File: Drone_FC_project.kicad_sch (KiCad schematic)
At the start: 1 part, among them U2 STM32F103C8Tx

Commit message: IMU
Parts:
- removed U2: STM32F103C8Tx, Package_QFP:LQFP-48_7x7mm_P0.5mm, symbol MCU_ST_STM32F1:STM32F103C8Tx
- added U2: STM32F411CCUx, Package_DFN_QFN:QFN-48-1EP_7x7mm_P0.5mm_EP5.6x5.6mm, symbol MCU_ST_STM32F4:STM32F411CCUx
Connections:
- new net: U2.23 (VSS), U2.35 (VSS), U2.47 (VSS), U2.49 (VSS)
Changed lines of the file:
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@@
 	(paper "A4")
 	(symbol
-		(lib_id "MCU_ST_STM32F1:STM32F103C8Tx")
-		(at 106.68 81.28 0)
+		(lib_id "MCU_ST_STM32F4:STM32F411CCUx")
+		(at 99.06 80.01 0)
 		(unit 1)
 		(body_style 1)
@@
 		(fields_autoplaced yes)
 		(property "Reference" "U2"
-			(at 111.3633 121.92 0)
-			(show_name no)
-			(do_not_autoplace no)
-			(effects
-				(font
-					(size 1.27 1.27)
-				)
-				(justify left)
-			)
-		)
-		(property "Value" "STM32F103C8Tx"
-			(at 111.3633 124.46 0)
-			(show_name no)
-			(do_not_autoplace no)
-			(effects
-				(font
-					(size 1.27 1.27)
-				)
-				(justify left)
-			)
-		)
-		(property "Footprint" "Package_QFP:LQFP-48_7x7mm_P0.5mm"
-			(at 91.44 119.38 0)
+			(at 103.7433 120.65 0)
+			(show_name no)
+			(do_not_autoplace no)
+			(effects
+				(font
+					(size 1.27 1.27)
+				)
+				(justify left)
+			)
+		)
+		(property "Value" "STM32F411CCUx"
+			(at 103.7433 123.19 0)
+			(show_name no)
+			(do_not_autoplace no)
+			(effects
+				(font
+					(size 1.27 1.27)
+				)
+				(justify left)
+			)
+		)
+		(property "Footprint" "Package_DFN_QFN:QFN-48-1EP_7x7mm_P0.5mm_EP5.6x5.6mm"
+			(at 83.82 118.11 0)
 			(hide yes)
 			(show_name no)
@@
 			)
 		)
-		(property "Datasheet" "https://www.st.com/resource/en/datasheet/stm32f103c8.pdf"
-			(at 106.68 81.28 0)
+		(property "Datasheet" "https://www.st.com/resource/en/datasheet/stm32f411cc.pdf"
+			(at 99.06 80.01 0)
 			(hide yes)
 			(show_name no)
@@
 			)
 		)
-		(property "Description" "STMicroelectronics Arm Cortex-M3 MCU, 64KB flash, 20KB RAM, 72 MHz, 2.0-3.6V, 37 GPIO, LQFP48"
-			(at 106.68 81.28 0)
+		(property "Description" "STMicroelectronics Arm Cortex-M4 MCU, 256KB flash, 128KB RAM, 100 MHz, 1.7-3.6V, 36 GPIO, UFQFPN48"
+			(at 99.06 80.01 0)
 			(hide yes)
 			(show_name no)
@@
 			)
 		)
+		(pin "21"
+		)
+		(pin "10"
+		)
+		(pin "22"
+		)
+		(pin "2"
+		)
+		(pin "11"
+		)
+		(pin "18"
+		)
+		(pin "27"
+		)
+		(pin "17"
+		)
+		(pin "8"
+		)
+		(pin "32"
+		)
+		(pin "30"
+		)
+		(pin "14"
+		)
+		(pin "1"
+		)
+		(pin "5"
+		)
+		(pin "7"
+		)
+		(pin "23"
+		)
+		(pin "24"
+		)
+		(pin "12"
+		)
+		(pin "9"
+		)
+		(pin "29"
+		)
+		(pin "20"
+		)
+		(pin "28"
+		)
+		(pin "16"
+		)
+		(pin "15"
+		)
+		(pin "19"
+		)
+		(pin "13"
+		)
+		(pin "26"
+		)
+		(pin "25"
+		)
+		(pin "6"
+		)
 		(pin "3"
 		)
-		(pin "8"
-		)
-		(pin "6"
-		)
-		(pin "5"
-		)
-		(pin "10"
-		)
 		(pin "4"
 		)
-		(pin "2"
-		)
-		(pin "12"
-		)
-		(pin "7"
-		)
-		(pin "11"
-		)
-		(pin "9"
-		)
-		(pin "1"
-		)
-		(pin "13"
-		)
-		(pin "15"
-		)
 		(pin "31"
 		)
-		(pin "23"
-		)
-		(pin "29"
-		)
-		(pin "16"
+		(pin "38"
+		)
+		(pin "46"
+		)
+		(pin "41"
+		)
+		(pin "47"
+		)
+		(pin "36"
+		)
+		(pin "34"
+		)
+		(pin "39"
+		)
+		(pin "42"
 		)
 		(pin "35"
 		)
+		(pin "48"
+		)
+		(pin "40"
+		)
+		(pin "49"
+		)
+		(pin "45"
+		)
+		(pin "43"
+		)
+		(pin "44"
+		)
+		(pin "33"
+		)
 		(pin "37"
-		)
-		(pin "18"
-		)
-		(pin "27"
-		)
-		(pin "32"
-		)
-		(pin "19"
-		)
-		(pin "38"
-		)
-		(pin "28"
-		)
-		(pin "43"
-		)
-		(pin "36"
-		)
-		(pin "39"
-		)
-		(pin "42"
-		)
-		(pin "20"
-		)
-		(pin "21"
-		)
-		(pin "41"
-		)
-		(pin "24"
-		)
-		(pin "40"
-		)
-		(pin "33"
-		)
-		(pin "45"
-		)
-		(pin "14"
-		)
-		(pin "44"
-		)
-		(pin "30"
-		)
-		(pin "25"
-		)
-		(pin "22"
-		)
-		(pin "17"
-		)
-		(pin "26"
-		)
-		(pin "34"
-		)
-		(pin "47"
-		)
-		(pin "48"
-		)
-		(pin "46"
 		)
 		(instances
@@
 	)
 	(sheet
-		(at 39.37 74.93)
+		(at 24.13 130.81)
 		(size 12.7 5.08)
 		(exclude_from_sim no)
@@
 		)
 		(property "Sheetname" "Battery and regulator"
-			(at 39.37 74.2184 0)
+			(at 24.13 130.0984 0)
 			(show_name no)
 			(do_not_autoplace no)
@@
 		)
 		(property "Sheetfile" "Battery_and_regulator.kicad_sch"
-			(at 39.37 80.5946 0)
-			(show_name no)
-			(do_not_autoplace no)
+			(at 24.13 136.4746 0)
+			(show_name no)
+			(do_not_autoplace no)

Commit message: Updated stm32
Updated stm32 and usb-c
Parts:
- removed U2: STM32F411CCUx, Package_DFN_QFN:QFN-48-1EP_7x7mm_P0.5mm_EP5.6x5.6mm, symbol MCU_ST_STM32F4:STM32F411CCUx
- added C1, C11, C2, C3, C4: 100n, Capacitor_SMD:C_0603_1608Metric, symbol Device:C
- added C10, C9: 1u, Package_TO_SOT_SMD:SOT-23-5, symbol Device:C
- added C12, C13: 10p, Capacitor_SMD:C_0603_1608Metric, symbol Device:C
- added C5: 1u, Package_SO:SOIC-8_3.9x4.9mm_P1.27mm, symbol Device:C
- added C6: 4.7u, Package_SO:SOIC-8_3.9x4.9mm_P1.27mm, symbol Device:C
- added C7: 100n, Package_SO:SOIC-8_3.9x4.9mm_P1.27mm, symbol Device:C
- added D5, D6: LED, symbol Device:LED
- added J5: Conn_01x04_Pin, Package_DIP:DIP-6_W7.62mm, symbol Connector:Conn_01x04_Pin
- added J6: USB_C_Receptacle, symbol Connector:USB_C_Receptacle_USB2.0_16P
- added R10, R9: 1k, symbol Device:R
- added R11, R12: 5k1, symbol Device:R
- added R13: 10k, Package_TO_SOT_SMD:SOT-23, symbol Device:R
- added SW2: SW_Push, Button_Switch_THT:SW_NKK_GW12LJP, symbol Switch:SW_Push
- added TP1, TP2: TestPoint, RF_Module:Atmel_ATSAMR21G18-MR210UA_NoRFPads, symbol Connector:TestPoint
- added U3: AP2112K-3.3TRG1, Package_TO_SOT_SMD:SOT-23-5, symbol Regulator_Linear:AP2112K-3.3
- added U4: STM32F411CEU6, Package_DFN_QFN:QFN-48-1EP_7x7mm_P0.5mm_EP5.6x5.6mm, symbol MCU_ST_STM32F4:STM32F411CEUx
- added Y1: 8MHz, symbol Device:Crystal_GND24
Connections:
- new net: D5.1 (K), R9.1
- new net: J6.B5 (CC2), R12.1
- new net: J6.A4 (VBUS), J6.A9 (VBUS), J6.B4 (VBUS), J6.B9 (VBUS)
- new net: J6.A5 (CC1), R11.1
- new net: J6.A6 (D+), J6.B6 (D+), U4.33 (PA12)
- new net: J6.A7 (D-), J6.B7 (D-), U4.32 (PA11)
- new net: D6.1 (K), R10.1
- new net: U4.23 (VSS), U4.35 (VSS), U4.47 (VSS), U4.49 (VSS)
- new net: TP1.1, U4.34 (PA13)
- new net: TP2.1, U4.37 (PA14)
- new net: C12.1, U4.5 (PH0), Y1.1
- new net: C13.1, U4.6 (PH1), Y1.3
- new net +3.3V: C1.1, C10.1, C2.1, C3.1, C4.1, C5.1, C6.1, C7.1, D5.2 (A), SW2.1, U3.5 (VOUT), U4.1 (VBAT), U4.24 (VDD), U4.36 (VDD), U4.48 (VDD), U4.9 (VDDA)
- new net +5V: D6.2 (A)
- new net +BATT: C9.1, J5.1 (Pin_1), J5.2 (Pin_2), U3.1 (VIN), U3.3 (EN)
- new net BOOT0: R13.1, SW2.2, U4.44 (BOOT0)
- new net GND: C1.2, C10.2, C11.2, C12.2, C13.2, C2.2, C3.2, C4.2, C5.2, C6.2, C7.2, C9.2, J5.3 (Pin_3), J5.4 (Pin_4), J6.A1 (GND), J6.A12 (GND), J6.B1 (GND), J6.B12 (GND), J6.SH (SHIELD), R10.2, R11.2, R12.2, R13.2, R9.2, U3.2 (GND), Y1.2 (G), Y1.4 (G)
- new net NRST: C11.1, U4.7 (NRST)
- no-connect marks 0 -> 3
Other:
- note added: "RED LEDs To inidicate 3.3V/5V is running"
- note added: "The pins that attach to the battery"
- note added: "Tie EN to HIGH"

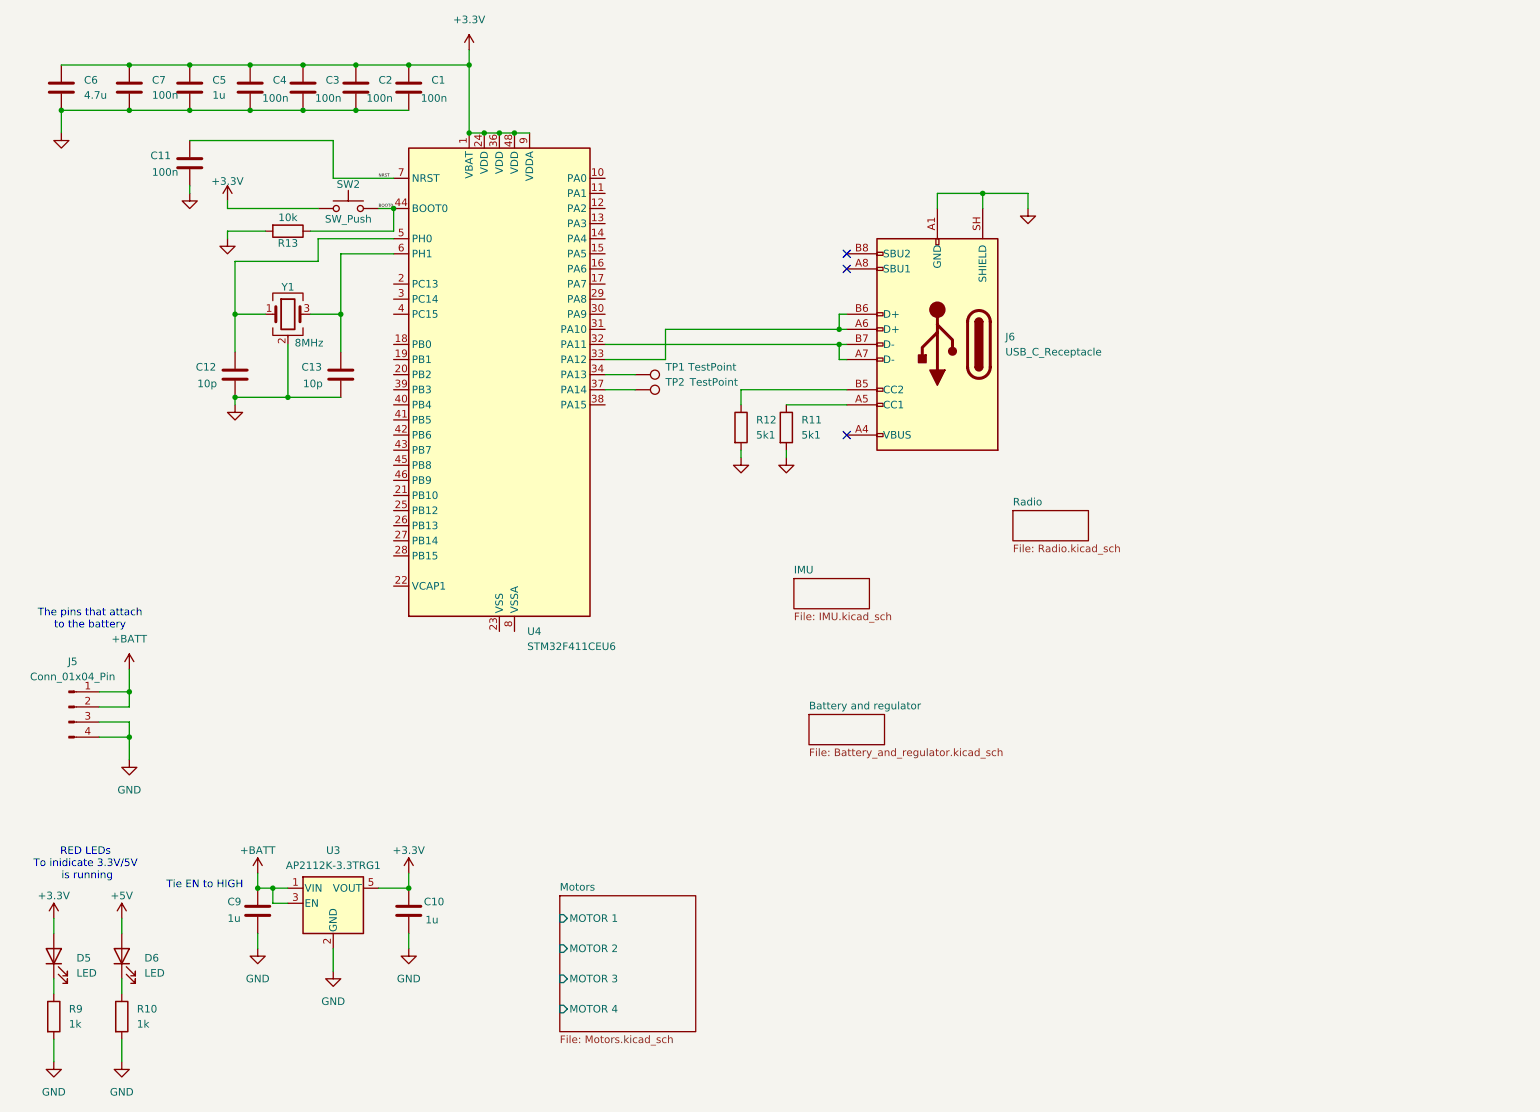
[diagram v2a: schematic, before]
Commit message: IMU, VBAT_Sense,
Fixed some decoupling issues, made the IMU into SPI mode. Wired all to stm32. Few updates on the appearances as well to make it look more organized.
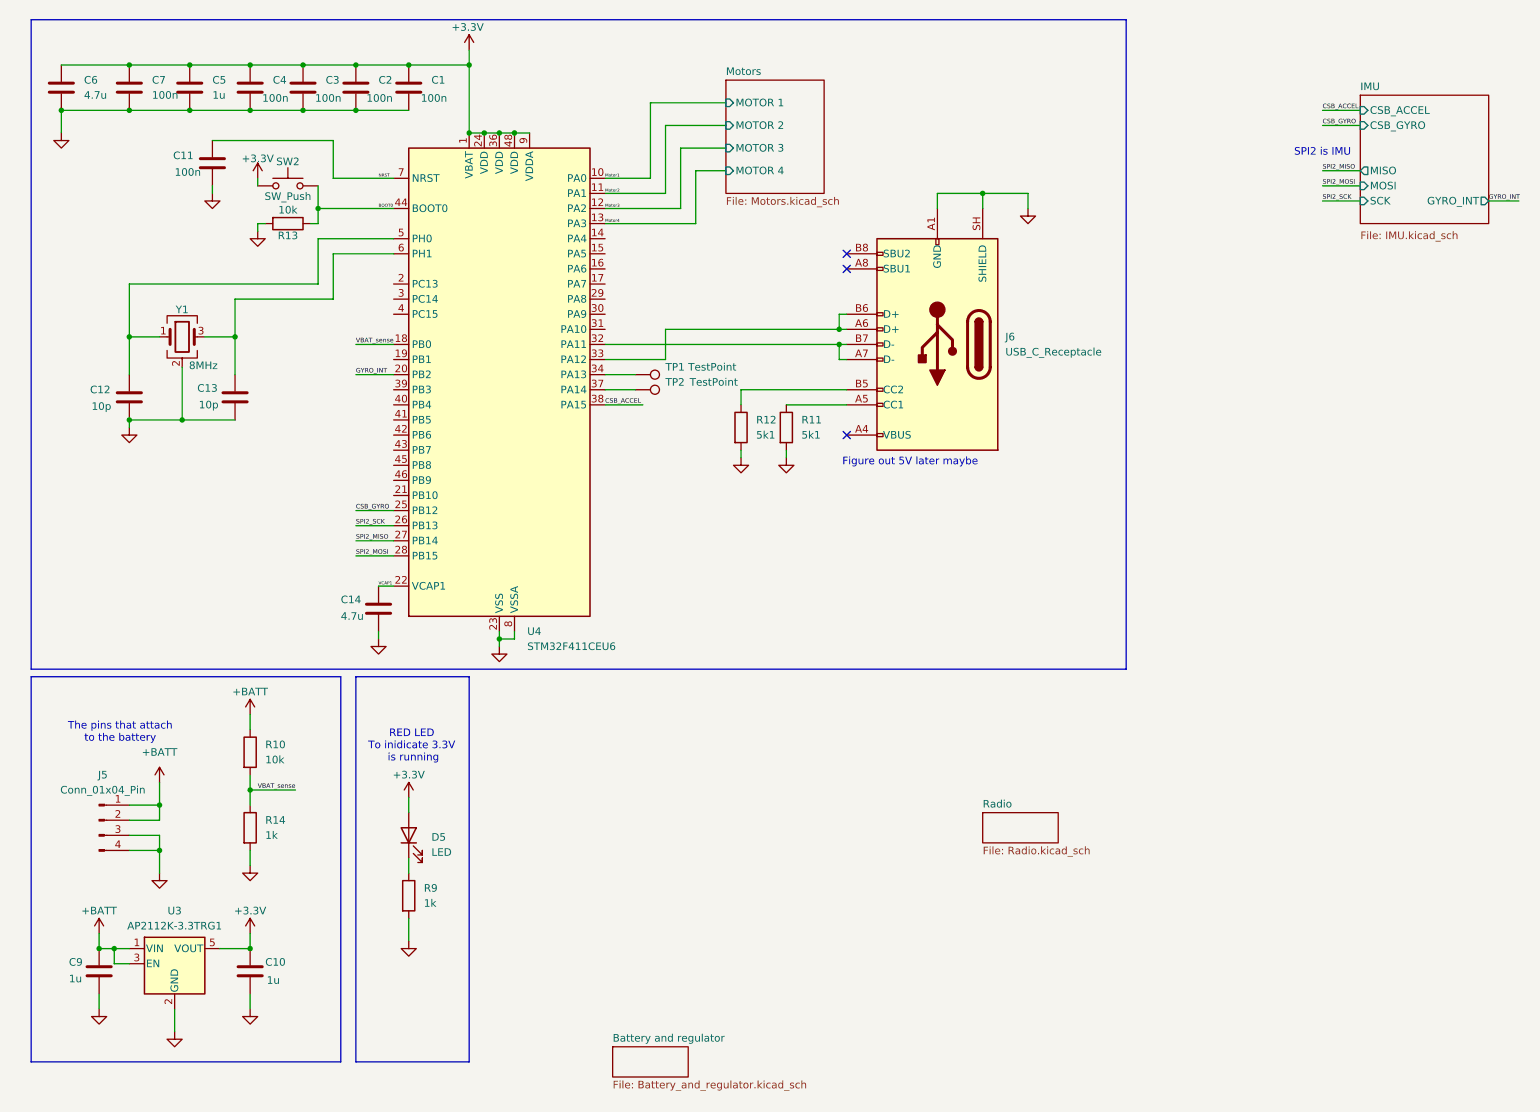
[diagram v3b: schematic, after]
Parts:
- removed D6: LED, symbol Device:LED
- added C14: 4.7u, Package_SO:SOIC-8_3.9x4.9mm_P1.27mm, symbol Device:C
- added R14: 1k, symbol Device:R
- R10: value 1k -> 10k
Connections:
- net +BATT: now also R10.1
- net GND: now also U4.23 (VSS), U4.35 (VSS), U4.47 (VSS), U4.49 (VSS), U4.8 (VSSA), C14.2, R14.2; no longer R10.2
- net Motor1: now reaches U4.10 (PA0)
- net Motor2: now reaches U4.11 (PA1)
- net Motor3: now reaches U4.12 (PA2)
- net Motor4: now reaches U4.13 (PA3)
- net VBAT_sense: now reaches U4.18 (PB0)
- net VBAT_sense: now also R10.2, R14.1
- net GYRO_INT: now reaches U4.20 (PB2)
- net VCAP1: now reaches U4.22 (VCAP1)
- net VCAP1: now also C14.1
- net CSB_GYRO: now reaches U4.25 (PB12)
- net SPI2_SCK: now reaches U4.26 (PB13)
- net SPI2_MISO: now reaches U4.27 (PB14)
- net SPI2_MOSI: now reaches U4.28 (PB15)
- net CSB_ACCEL: now reaches U4.38 (PA15)
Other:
- sheet IMU ports: added CSB_ACCEL, CSB_GYRO, GYRO_INT, MISO, MOSI, SCK; removed none
- note added: "Figure out 5V later maybe"
- note added: "RED LED To inidicate 3.3V is running"
- note added: "SPI2 is IMU"
- note removed: "RED LEDs To inidicate 3.3V/5V is running"
- note removed: "Tie EN to HIGH"
- moved on the sheet: C10, C11, C12, C13, C9, D5, J5, R13, R9, SW2, U3, Y1

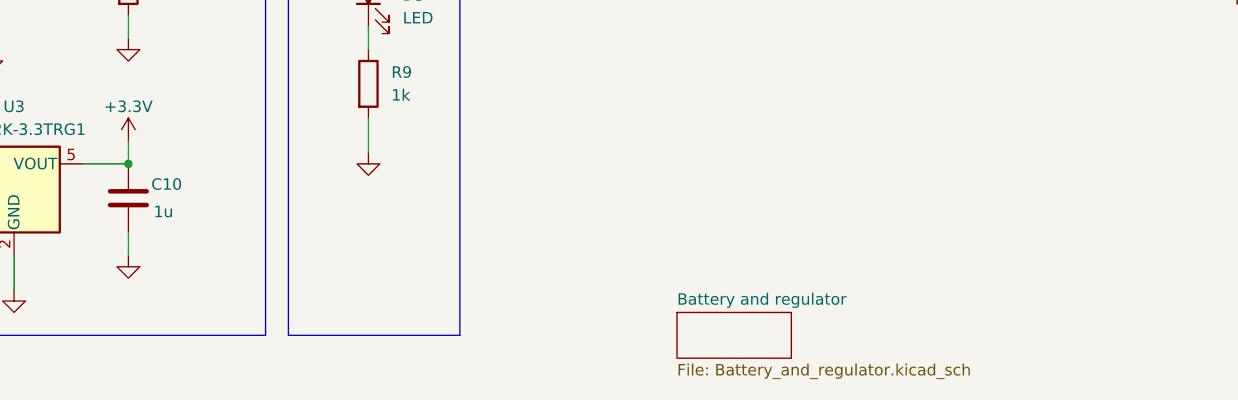
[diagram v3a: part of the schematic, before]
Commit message: radio starting
Radio start + changes to the root name
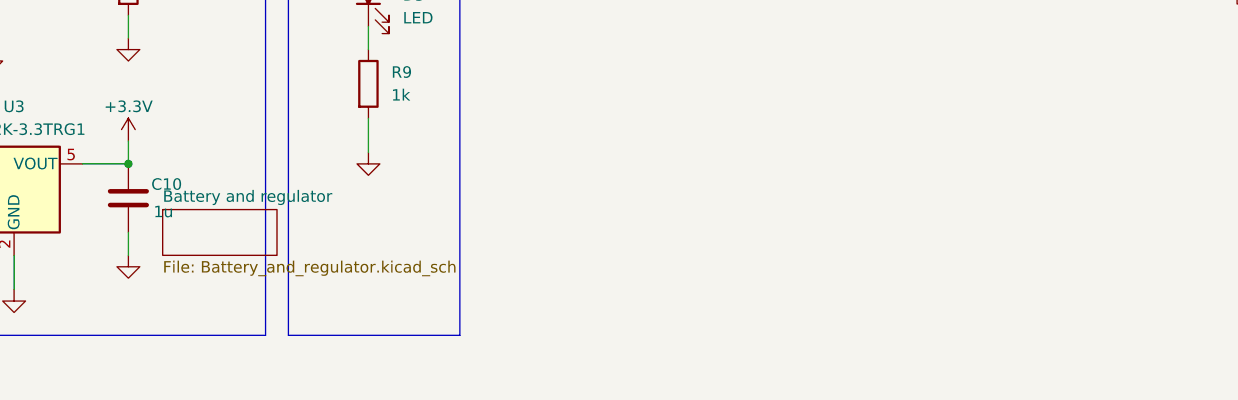
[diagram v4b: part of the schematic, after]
